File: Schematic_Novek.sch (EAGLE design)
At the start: 13 parts, among them IC1 STM32F10XCXT6

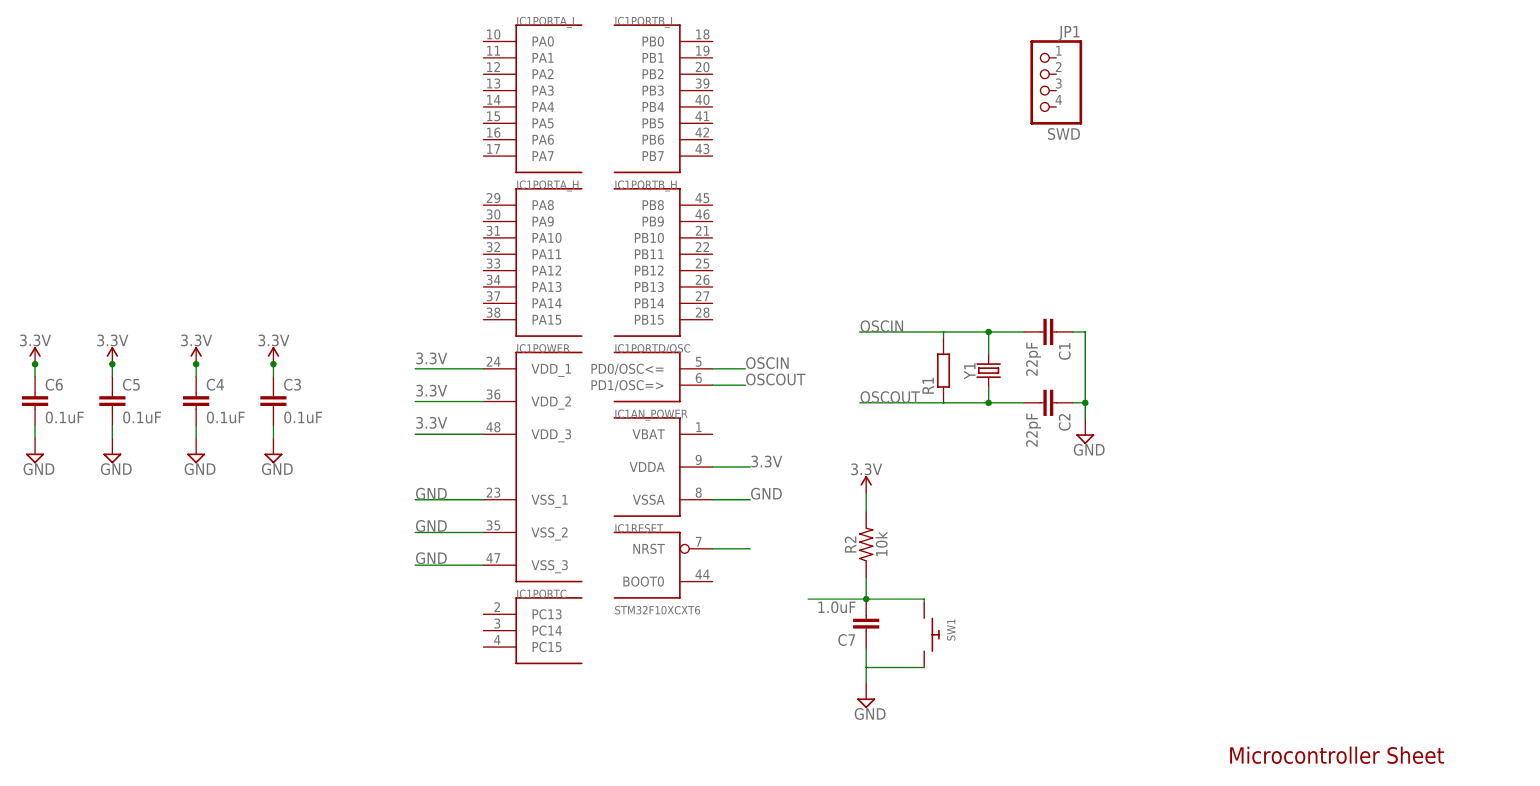
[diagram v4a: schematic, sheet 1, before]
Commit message: Adds header pin for debugger
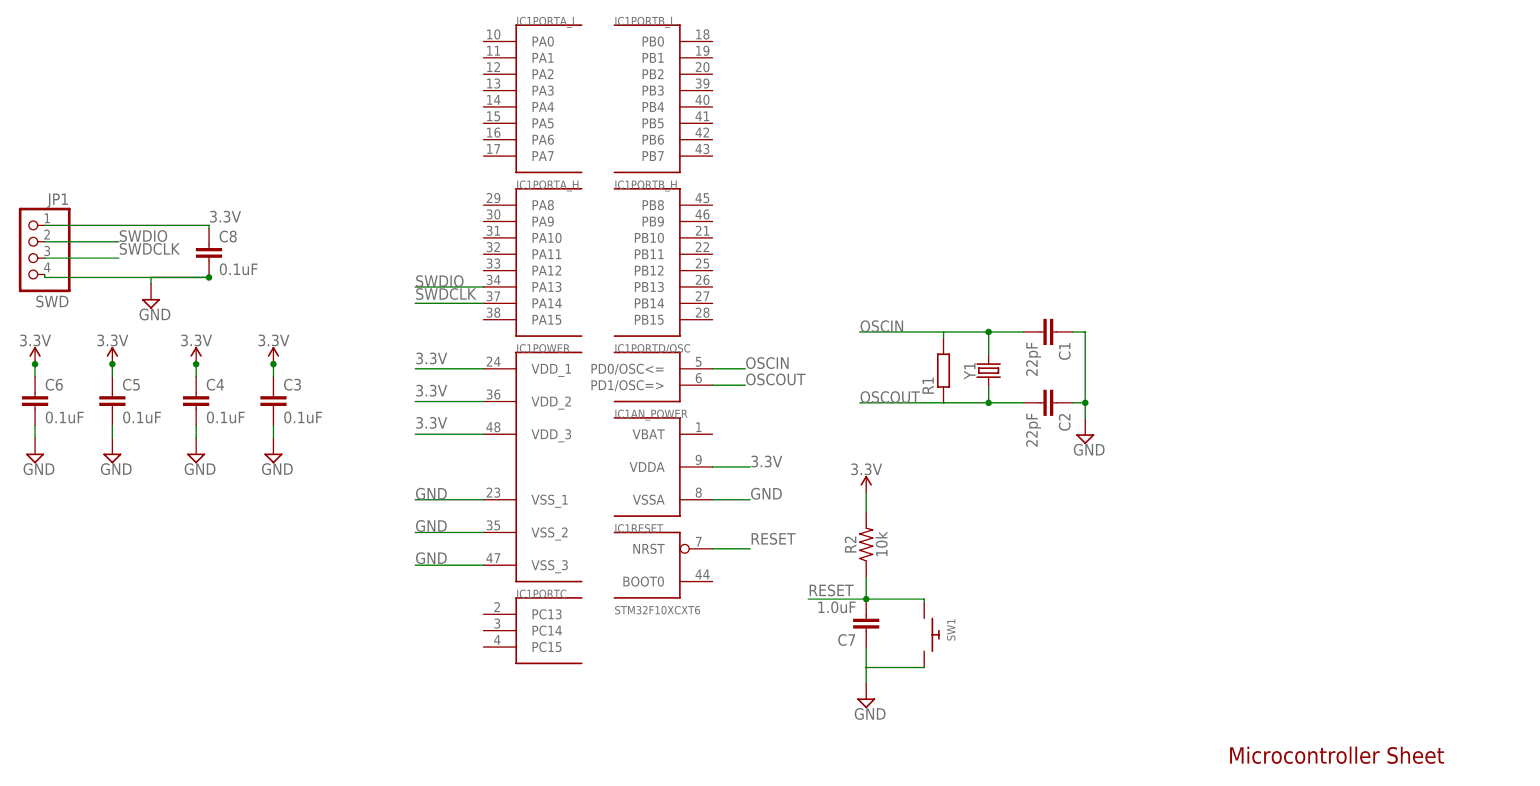
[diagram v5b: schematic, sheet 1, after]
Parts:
- added C8: 0.1uF, SparkFun-Capacitors:0.1UF-0603-25V-(+80/-20%)
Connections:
- removed net N$1: C7.2, R2.1, SW1.P$1
- removed net N$2: IC1RESET.NRST
- new net RESET: C7.2, IC1RESET.NRST, R2.1, SW1.P$1
- new net SWDCLK: IC1PORTA_H.PA14, JP1.3
- new net SWDIO: IC1PORTA_H.PA13, JP1.2
- net 3.3V: now also C8.1, JP1.1
- net GND: now also C8.2, JP1.4
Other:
- moved on the sheet: JP1
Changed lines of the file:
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@@
 <part name="SW1" library="adafruit" deviceset="SWITCH_PUSHBUTTON" device="C&amp;K_KSS"/>
 <part name="SUPPLY11" library="supply2" deviceset="GND" device=""/>
+<part name="C8" library="SparkFun-Capacitors" deviceset="0.1UF" device="-0603-25V-(+80/-20%)" value="0.1uF"/>
+<part name="SUPPLY12" library="supply2" deviceset="GND" device=""/>
 </parts>
 <sheets>
@@
 <attribute name="VALUE" x="176.302" y="77.19" size="1.778" layer="96" rot="R90"/>
 </instance>
-<instance part="JP1" gate="A" x="187.96" y="124.46" smashed="yes" rot="MR0">
-<attribute name="NAME" x="194.31" y="132.715" size="1.778" layer="95" rot="MR0"/>
-<attribute name="VALUE" x="194.31" y="116.84" size="1.778" layer="96" rot="MR0"/>
+<instance part="JP1" gate="A" x="30.96" y="98.46" smashed="yes" rot="MR0">
+<attribute name="NAME" x="37.31" y="106.715" size="1.778" layer="95" rot="MR0"/>
+<attribute name="VALUE" x="37.31" y="90.84" size="1.778" layer="96" rot="MR0"/>
 </instance>
 <instance part="C3" gate="G$1" x="69" y="75" smashed="yes">
@@
 <instance part="SUPPLY11" gate="GND" x="161" y="30" smashed="yes">
 <attribute name="VALUE" x="159.095" y="26.825" size="1.778" layer="96"/>
+</instance>
+<instance part="C8" gate="G$1" x="59" y="98" smashed="yes">
+<attribute name="NAME" x="60.524" y="100.921" size="1.778" layer="95" font="vector"/>
+<attribute name="VALUE" x="60.524" y="95.841" size="1.778" layer="96" font="vector"/>
+</instance>
+<instance part="SUPPLY12" gate="GND" x="50" y="92" smashed="yes">
+<attribute name="VALUE" x="48.095" y="88.825" size="1.778" layer="96"/>
 </instance>
 </instances>
@@
 <wire x1="161" y1="32.54" x2="161" y2="34.92" width="0.1524" layer="91"/>
 </segment>
+<segment>
+<pinref part="JP1" gate="A" pin="4"/>
+<pinref part="C8" gate="G$1" pin="2"/>
+<wire x1="59" y1="95.46" x2="33.5" y2="95.46" width="0.1524" layer="91"/>
+<wire x1="33.5" y1="95.46" x2="33.5" y2="95.92" width="0.1524" layer="91"/>
+<pinref part="SUPPLY12" gate="GND" pin="GND"/>
+<wire x1="59" y1="95.46" x2="50" y2="95.46" width="0.1524" layer="91"/>
+<wire x1="50" y1="95.46" x2="50" y2="94.54" width="0.1524" layer="91"/>
+<junction x="59" y="95.46"/>
+</segment>
 </net>
 <net name="3.3V" class="0">
@@
 <wire x1="161" y1="62" x2="161" y2="59.08" width="0.1524" layer="91"/>
 </segment>
-</net>
-<net name="N$1" class="0">
+<segment>
+<pinref part="JP1" gate="A" pin="1"/>
+<pinref part="C8" gate="G$1" pin="1"/>
+<wire x1="33.5" y1="103.54" x2="59" y2="103.54" width="0.1524" layer="91"/>
+<wire x1="59" y1="103.54" x2="59" y2="103.08" width="0.1524" layer="91"/>
+<label x="59" y="104" size="1.778" layer="95"/>
+</segment>
+</net>
+<net name="RESET" class="0">
+<segment>
+<pinref part="IC1" gate="RESET" pin="NRST"/>
+<wire x1="137.16" y1="53.34" x2="143" y2="53.34" width="0.1524" layer="91"/>
+<label x="143" y="54" size="1.778" layer="95"/>
+</segment>
 <segment>
 <pinref part="R2" gate="G$1" pin="1"/>
@@
 <junction x="161" y="45.54"/>
 <wire x1="161" y1="45.54" x2="152" y2="45.54" width="0.1524" layer="91"/>
-</segment>
-</net>
-<net name="N$2" class="0">
-<segment>
-<pinref part="IC1" gate="RESET" pin="NRST"/>
-<wire x1="137.16" y1="53.34" x2="143" y2="53.34" width="0.1524" layer="91"/>
-</segment>
-</net>
+<label x="152" y="46" size="1.778" layer="95"/>
+</segment>
+</net>
+<net name="SWDCLK" class="0">
+<segment>
+<pinref part="IC1" gate="PORTA_H" pin="PA14"/>
+<wire x1="101.6" y1="91.44" x2="91" y2="91.44" width="0.1524" layer="91"/>
+<label x="91" y="92" size="1.778" layer="95"/>
+</segment>
+<segment>
+<pinref part="JP1" gate="A" pin="3"/>
+<wire x1="33.5" y1="98.46" x2="45" y2="98.46" width="0.1524" layer="91"/>
+<label x="45" y="99" size="1.778" layer="95"/>
+</segment>
+</net>
+<net name="SWDIO" class="0">
+<segment>
+<pinref part="IC1" gate="PORTA_H" pin="PA13"/>
+<wire x1="101.6" y1="93.98" x2="91" y2="93.98" width="0.1524" layer="91"/>
+<label x="91" y="94" size="1.778" layer="95"/>
+</segment>
+<segment>
+<pinref part="JP1" gate="A" pin="2"/>
+<wire x1="33.5" y1="101" x2="45" y2="101" width="0.1524" layer="91"/>
+<label x="45" y="101" size="1.778" layer="95"/>
+</segment>
+</net>

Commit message: Adds header pin to switch between the different bootable memories
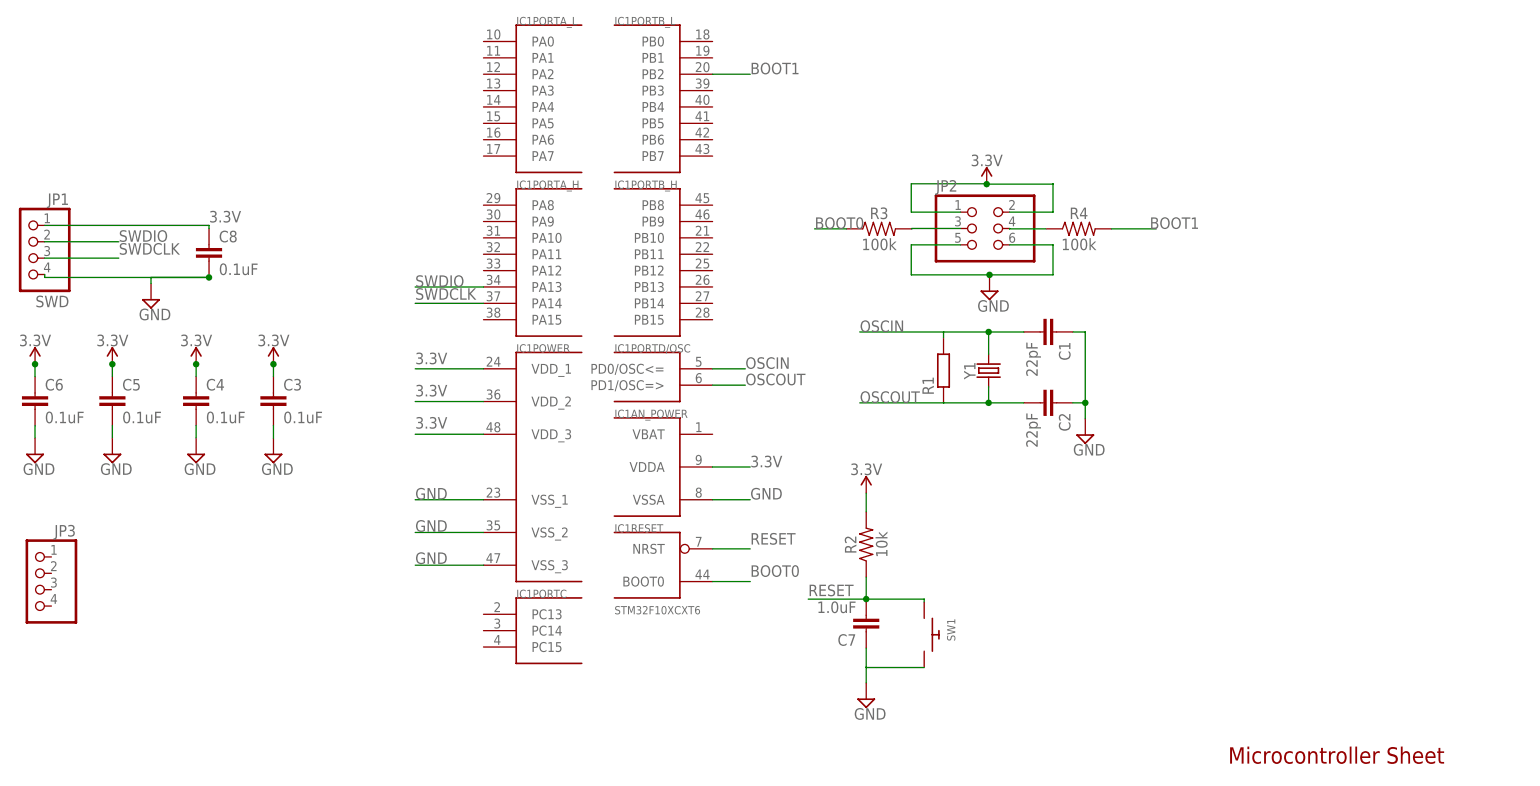
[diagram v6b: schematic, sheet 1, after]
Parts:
- added JP2: (no value), pinhead:PINHD-2X3
- added JP3: (no value), pinhead:PINHD-1X4
- added R3, R4: 100k, SparkFun-Resistors:100KOHM-0603-1/10W-1%
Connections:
- new net BOOT0: IC1RESET.BOOT0, R3.1
- new net BOOT1: IC1PORTB_L.PB2, R4.2
- new net N$3: JP2.3, R3.2
- new net N$4: JP2.4, R4.1
- net 3.3V: now also JP2.1, JP2.2
- net GND: now also JP2.5, JP2.6
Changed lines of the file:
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@@
 <setting verticaltext="up"/>
 </settings>
-<grid distance="1" unitdist="mm" unit="mm" style="lines" multiple="1" display="yes" altdistance="1" altunitdist="mm" altunit="mm"/>
+<grid distance="1" unitdist="mm" unit="mm" style="dots" multiple="1" display="yes" altdistance="1" altunitdist="mm" altunit="mm"/>
 <layers>
 <layer number="1" name="Top" color="4" fill="1" visible="no" active="no"/>
@@
 <part name="C8" library="SparkFun-Capacitors" deviceset="0.1UF" device="-0603-25V-(+80/-20%)" value="0.1uF"/>
 <part name="SUPPLY12" library="supply2" deviceset="GND" device=""/>
+<part name="JP2" library="pinhead" deviceset="PINHD-2X3" device=""/>
+<part name="SUPPLY13" library="SparkFun-PowerSymbols" deviceset="3.3V" device=""/>
+<part name="SUPPLY14" library="supply2" deviceset="GND" device=""/>
+<part name="R3" library="SparkFun-Resistors" deviceset="100KOHM" device="-0603-1/10W-1%" value="100k"/>
+<part name="R4" library="SparkFun-Resistors" deviceset="100KOHM" device="-0603-1/10W-1%" value="100k"/>
+<part name="JP3" library="pinhead" library_urn="urn:adsk.eagle:library:325" deviceset="PINHD-1X4" device="" package3d_urn="urn:adsk.eagle:package:22407/2"/>
 </parts>
 <sheets>
@@
 <attribute name="VALUE" x="48.095" y="88.825" size="1.778" layer="96"/>
 </instance>
+<instance part="JP2" gate="A" x="178.18" y="103.06" smashed="yes">
+<attribute name="NAME" x="171.83" y="108.775" size="1.778" layer="95"/>
+<attribute name="VALUE" x="171.83" y="95.44" size="1.778" layer="96"/>
+</instance>
+<instance part="SUPPLY13" gate="G$1" x="179.7" y="109.94" smashed="yes">
+<attribute name="VALUE" x="179.7" y="112.734" size="1.778" layer="96" align="bottom-center"/>
+</instance>
+<instance part="SUPPLY14" gate="GND" x="180.14" y="93.32" smashed="yes">
+<attribute name="VALUE" x="178.235" y="90.145" size="1.778" layer="96"/>
+</instance>
+<instance part="R3" gate="G$1" x="163" y="103" smashed="yes">
+<attribute name="NAME" x="163" y="104.524" size="1.778" layer="95" font="vector" align="bottom-center"/>
+<attribute name="VALUE" x="163" y="101.476" size="1.778" layer="96" font="vector" align="top-center"/>
+</instance>
+<instance part="R4" gate="G$1" x="194" y="103" smashed="yes">
+<attribute name="NAME" x="194" y="104.524" size="1.778" layer="95" font="vector" align="bottom-center"/>
+<attribute name="VALUE" x="194" y="101.476" size="1.778" layer="96" font="vector" align="top-center"/>
+</instance>
+<instance part="JP3" gate="A" x="32" y="47" smashed="yes" rot="MR0">
+<attribute name="NAME" x="38.35" y="55.255" size="1.778" layer="95" rot="MR0"/>
+<attribute name="VALUE" x="38.35" y="39.38" size="1.778" layer="96" rot="MR0"/>
+</instance>
 </instances>
 <busses>
@@
 <junction x="59" y="95.46"/>
 </segment>
+<segment>
+<pinref part="JP2" gate="A" pin="5"/>
+<wire x1="175.64" y1="100.52" x2="168" y2="100.52" width="0.1524" layer="91"/>
+<wire x1="168" y1="100.52" x2="168" y2="95.86" width="0.1524" layer="91"/>
+<pinref part="SUPPLY14" gate="GND" pin="GND"/>
+<wire x1="168" y1="95.86" x2="180.14" y2="95.86" width="0.1524" layer="91"/>
+<wire x1="180.14" y1="95.86" x2="190" y2="95.86" width="0.1524" layer="91"/>
+<wire x1="190" y1="95.86" x2="190" y2="100.52" width="0.1524" layer="91"/>
+<junction x="180.14" y="95.86"/>
+<pinref part="JP2" gate="A" pin="6"/>
+<wire x1="190" y1="100.52" x2="183.26" y2="100.52" width="0.1524" layer="91"/>
+</segment>
 </net>
 <net name="3.3V" class="0">
@@
 <wire x1="59" y1="103.54" x2="59" y2="103.08" width="0.1524" layer="91"/>
 <label x="59" y="104" size="1.778" layer="95"/>
+</segment>
+<segment>
+<pinref part="JP2" gate="A" pin="1"/>
+<wire x1="175.64" y1="105.6" x2="168" y2="105.6" width="0.1524" layer="91"/>
+<wire x1="168" y1="105.6" x2="168" y2="110" width="0.1524" layer="91"/>
+<pinref part="SUPPLY13" gate="G$1" pin="3.3V"/>
+<wire x1="168" y1="110" x2="179.7" y2="110" width="0.1524" layer="91"/>
+<wire x1="179.7" y1="110" x2="179.7" y2="109.94" width="0.1524" layer="91"/>
+<wire x1="179.7" y1="109.94" x2="190" y2="109.94" width="0.1524" layer="91"/>
+<wire x1="190" y1="109.94" x2="190" y2="110" width="0.1524" layer="91"/>
+<junction x="179.7" y="109.94"/>
+<pinref part="JP2" gate="A" pin="2"/>
+<wire x1="190" y1="109.94" x2="190" y2="105.6" width="0.1524" layer="91"/>
+<wire x1="190" y1="105.6" x2="183.26" y2="105.6" width="0.1524" layer="91"/>
 </segment>
 </net>
@@
 </segment>
 </net>
+<net name="N$3" class="0">
+<segment>
+<pinref part="R3" gate="G$1" pin="2"/>
+<pinref part="JP2" gate="A" pin="3"/>
+<wire x1="168.08" y1="103" x2="168.08" y2="103.06" width="0.1524" layer="91"/>
+<wire x1="168.08" y1="103.06" x2="175.64" y2="103.06" width="0.1524" layer="91"/>
+</segment>
+</net>
+<net name="N$4" class="0">
+<segment>
+<pinref part="JP2" gate="A" pin="4"/>
+<pinref part="R4" gate="G$1" pin="1"/>
+<wire x1="183.26" y1="103.06" x2="183.26" y2="103" width="0.1524" layer="91"/>
+<wire x1="183.26" y1="103" x2="188.92" y2="103" width="0.1524" layer="91"/>
+</segment>
+</net>
+<net name="BOOT0" class="0">
+<segment>
+<pinref part="IC1" gate="RESET" pin="BOOT0"/>
+<wire x1="137.16" y1="48.26" x2="143" y2="48.26" width="0.1524" layer="91"/>
+<label x="143" y="49" size="1.778" layer="95"/>
+</segment>
+<segment>
+<pinref part="R3" gate="G$1" pin="1"/>
+<wire x1="157.92" y1="103" x2="153" y2="103" width="0.1524" layer="91"/>
+<label x="153" y="103" size="1.778" layer="95"/>
+</segment>
+</net>
+<net name="BOOT1" class="0">
+<segment>
+<pinref part="IC1" gate="PORTB_L" pin="PB2"/>
+<wire x1="137.16" y1="127" x2="143" y2="127" width="0.1524" layer="91"/>
+<label x="143" y="127" size="1.778" layer="95"/>
+</segment>
+<segment>
+<pinref part="R4" gate="G$1" pin="2"/>
+<wire x1="199.08" y1="103" x2="206" y2="103" width="0.1524" layer="91"/>
+<label x="205" y="103" size="1.778" layer="95"/>
+</segment>
+</net>

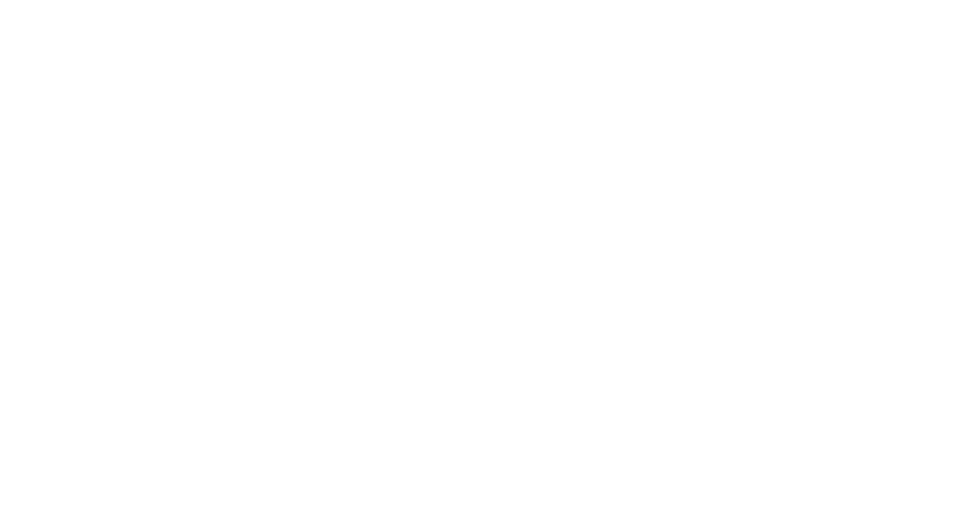
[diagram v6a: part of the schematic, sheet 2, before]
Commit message: Adds bq21040
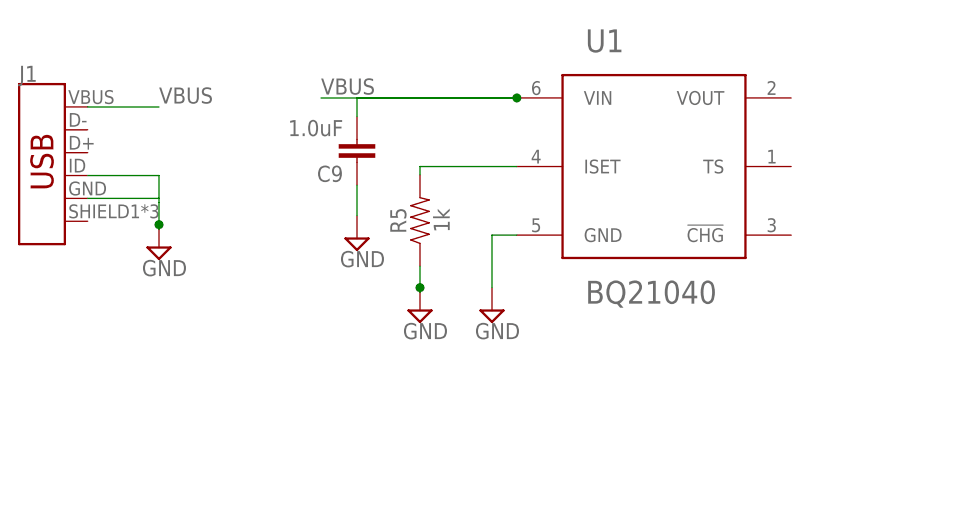
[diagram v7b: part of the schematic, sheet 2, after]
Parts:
- added C9: 1.0uF, SparkFun-Capacitors:1.0UF-0603-16V-10%
- added J1: (no value), SparkFun-Connectors:USB_MICRO-B_FEMALE-SMT
- added R5: 1k, SparkFun-Resistors:1KOHM-0603-1/10W-1%
- added U1: BQ21040, bq21040:BQ21040
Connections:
- new net 5V: JP3.3
- new net FTDI_RX: IC1PORTA_H.PA9, JP3.1
- new net FTDI_TX: IC1PORTA_H.PA10, JP3.2
- new net N$1: R5.2, U1.ISET
- new net VBUS: C9.2, J1.VBUS, U1.VIN
- net GND: now also C9.1, J1.GND, J1.ID, JP3.4, R5.1, U1.GND
